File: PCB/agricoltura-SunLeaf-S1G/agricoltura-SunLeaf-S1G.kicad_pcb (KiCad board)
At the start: 2 copper layers, 120 x 40 mm, 84 parts, among them M1 SPSGRFC-915, Q1 DMP3125L-7, Q2 DMP3125L-7, SW1 TL3301NF260QG, T1 BU2032SM-JJ-GTR, T10 BM04B-SRSS-TB(LF)(SN), T11 BM04B-SRSS-TB(LF)(SN), T12 BM04B-SRSS-TB(LF)(SN), T13 BM04B-SRSS-TB(LF)(SN), T14 BM04B-SRSS-TB(LF)(SN), T15 BM04B-SRSS-TB(LF)(SN), T16 BM04B-SRSS-TB(LF)(SN), T17 BM04B-SRSS-TB(LF)(SN), T2 20021121-00010C4LF, T3 0675031020, T4 S2B-PH-K-S(LF)(SN), T5 S3B-PH-K-S(LF)(SN), T6 BM04B-SRSS-TB(LF)(SN), T7 BM04B-SRSS-TB(LF)(SN), T8 BM04B-SRSS-TB(LF)(SN), T9 BM04B-SRSS-TB(LF)(SN), U1 STM32F446RET6, U2 BQ24210DQCT, U3 AZ1117CR-3.3TRG1, U4 TCA9548APWR, U5 74HC4052D, X1 ABM3B-8.000MHZ-B2-T, X2 ABS07-32.768KHZ-9-T

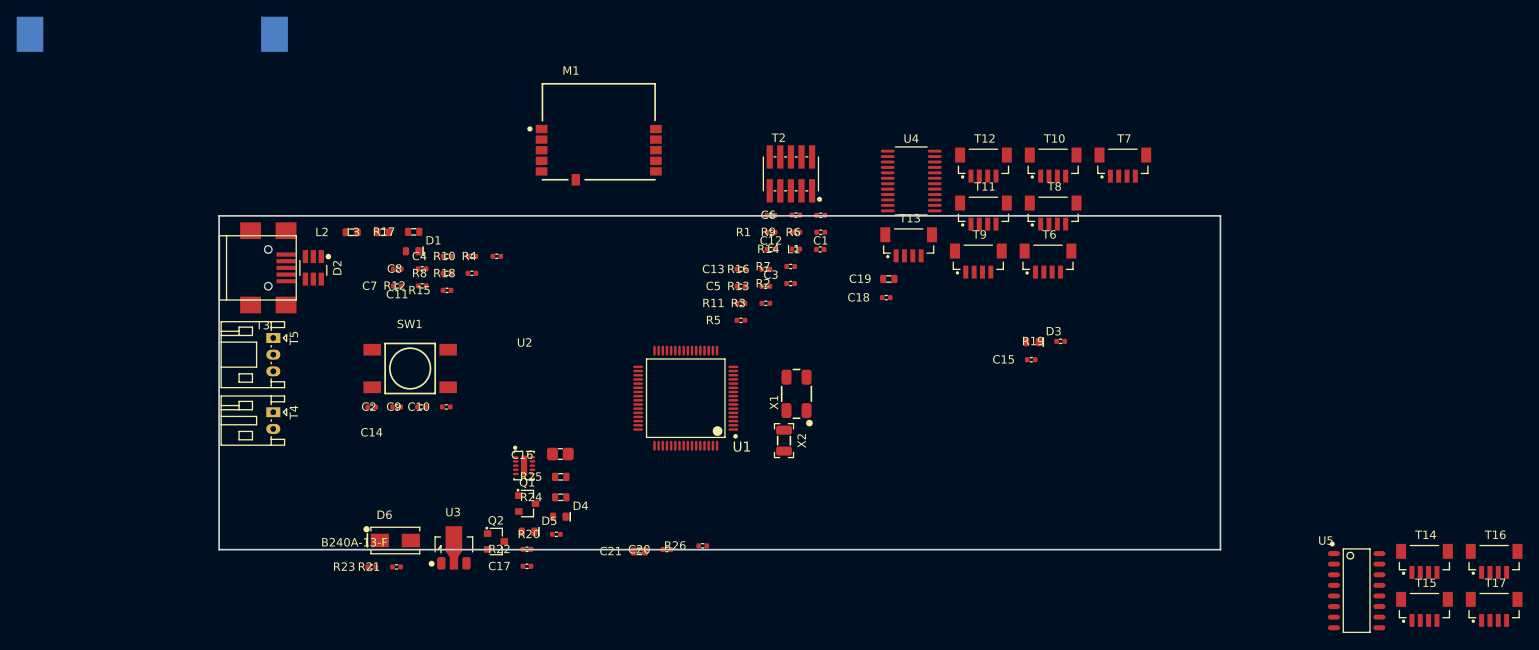
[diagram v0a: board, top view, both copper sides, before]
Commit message: PCB Progress
added TVS diodes fo QWIIC connector serial signals. Did more routing overall.
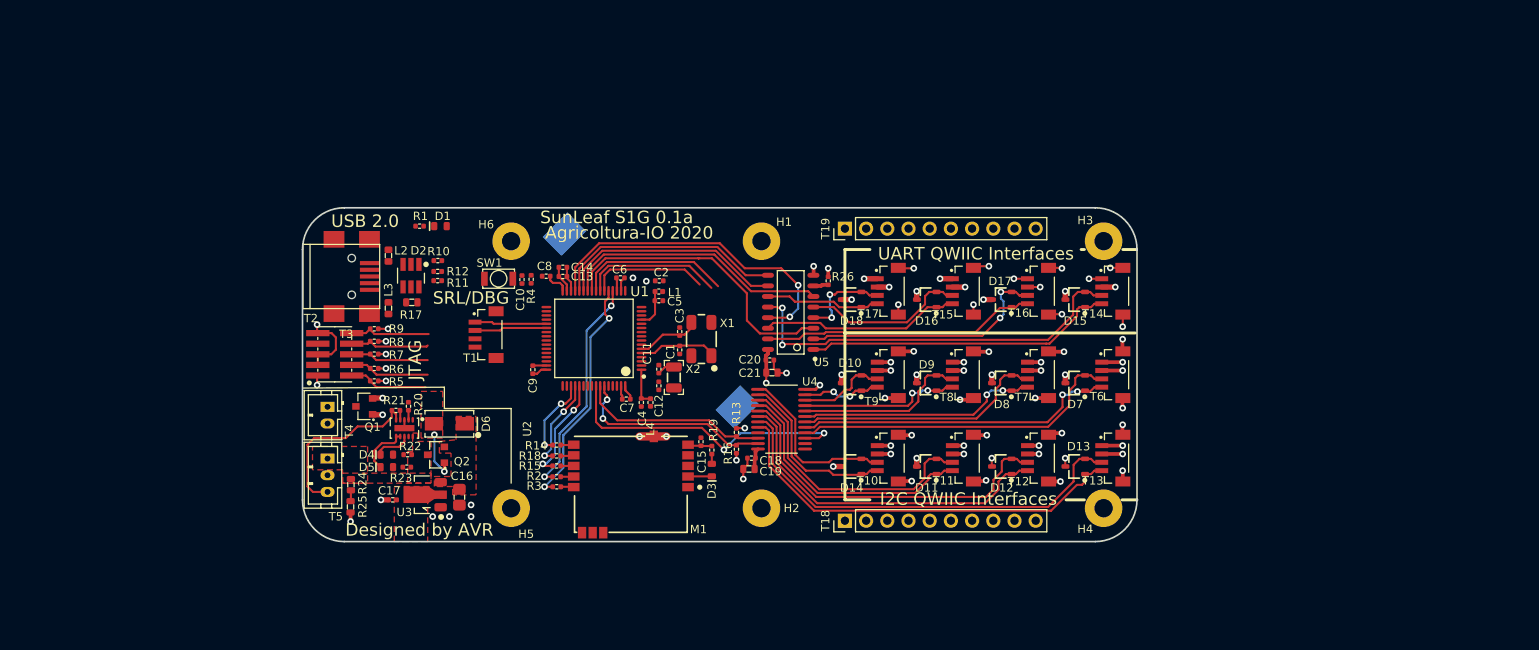
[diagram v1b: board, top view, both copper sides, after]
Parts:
- added D10: PESD3V3L2BT,215, AVR-KiCAD-Lib-Diodes:SOT-23, F.Cu at (165.8, 91.0)
- added D11: PESD3V3L2BT,215, AVR-KiCAD-Lib-Diodes:SOT-23, F.Cu at (174.8, 101.0)
- added D12: PESD3V3L2BT,215, AVR-KiCAD-Lib-Diodes:SOT-23, F.Cu at (183.8, 101.0)
- added D13: PESD3V3L2BT,215, AVR-KiCAD-Lib-Diodes:SOT-23, F.Cu at (192.6, 101.0)
- added D14: PESD3V3L2BT,215, AVR-KiCAD-Lib-Diodes:SOT-23, F.Cu at (165.8, 101.0)
- added D15: PESD3V3L2BT,215, AVR-KiCAD-Lib-Diodes:SOT-23, F.Cu at (192.6, 81.0)
- added D16: PESD3V3L2BT,215, AVR-KiCAD-Lib-Diodes:SOT-23, F.Cu at (174.8, 81.0)
- added D17: PESD3V3L2BT,215, AVR-KiCAD-Lib-Diodes:SOT-23, F.Cu at (183.8, 81.0)
- added D18: PESD3V3L2BT,215, AVR-KiCAD-Lib-Diodes:SOT-23, F.Cu at (165.8, 81.0)
- added D7: PESD3V3L2BT,215, AVR-KiCAD-Lib-Diodes:SOT-23, F.Cu at (192.6, 91.0)
- added D8: PESD3V3L2BT,215, AVR-KiCAD-Lib-Diodes:SOT-23, F.Cu at (183.8, 91.0)
- added D9: PESD3V3L2BT,215, AVR-KiCAD-Lib-Diodes:SOT-23, F.Cu at (174.8, 91.0)
- added H1: M2_Plated_Hole, AVR-KiCAD-Lib-Holes_Fasteners:M2_HOLE, F.Cu at (155.0, 74.0)
- added H2: M2_Plated_Hole, AVR-KiCAD-Lib-Holes_Fasteners:M2_HOLE, F.Cu at (155.0, 106.0)
- added H3: M2_Plated_Hole, AVR-KiCAD-Lib-Holes_Fasteners:M2_HOLE, F.Cu at (196.0, 74.0)
- added H4: M2_Plated_Hole, AVR-KiCAD-Lib-Holes_Fasteners:M2_HOLE, F.Cu at (196.0, 106.0)
- added H5: M2_Plated_Hole, AVR-KiCAD-Lib-Holes_Fasteners:M2_HOLE, F.Cu at (125.0, 106.0)
- added H6: M2_Plated_Hole, AVR-KiCAD-Lib-Holes_Fasteners:M2_HOLE, F.Cu at (125.0, 74.0)
- added L4: BLM15HG601SN1D, AVR-KiCAD-Lib-Inductors:BLM15HG601SN1D, F.Cu at (141.7, 93.3)
- added T18: PPTC101LFBN-RC, AVR-KiCAD-Lib-Connectors:Female_Header_Straight_1x10_Pitch2.54mm, F.Cu at (165.0, 107.5)
- added T19: PPTC101LFBN-RC, AVR-KiCAD-Lib-Connectors:Female_Header_Straight_1x10_Pitch2.54mm, F.Cu at (165.0, 72.5)
- added T20: BU2032SM-JJ-GTR, AVR-KiCAD-Lib-Battery-Holders:BU2032SM-JJ-GTR, B.Cu at (141.8, 83.5)
- M1: value SPSGRFC-915 -> SPSGRF-915
- SW1: value TL3301NF260QG -> B3U-1000P; footprint AVR-KiCAD-Lib-Mech-Switches:TL3301NF260QG -> AVR-KiCAD-Lib-Mech-Switches:B3U-1000P
- T1: value BU2032SM-JJ-GTR -> BM04B-SRSS-TB(LF)(SN); footprint AVR-KiCAD-Lib-Battery-Holders:BU2032SM-JJ-GTR -> AVR-KiCAD-Lib-Connectors:CONN_BM04B-SRSS-TB(LF)(SN); moved to F.Cu
- T4: value S2B-PH-K-S(LF)(SN) -> B2B-PH-K-S(LF)(SN); footprint AVR-KiCAD-Lib-Connectors:S2B-PH-K-S(LF)(SN) -> AVR-KiCAD-Lib-Connectors:B2B-PH-K-S(LF)(SN)
- T5: value S3B-PH-K-S(LF)(SN) -> B3B-PH-K-S(LF)(SN); footprint AVR-KiCAD-Lib-Connectors:S3B-PH-K-S(LF)(SN) -> AVR-KiCAD-Lib-Connectors:B3B-PH-K-S(LF)(SN)
- moved T17 82.0 mm to (170.2, 80.0), turned to 270 degrees
- moved U5 75.6 mm to (158.5, 82.5), turned to 180 degrees
- moved T15 67.1 mm to (179.2, 80.0), turned to 270 degrees
- moved T16 63.5 mm to (188.2, 80.0), turned to 270 degrees
- moved T2 58.8 mm to (103.9, 87.6), turned to 270 degrees
- moved R6 55.9 mm to (108.6, 89.2), turned to 180 degrees
- moved T1 53.8 mm to (122.0, 85.2), turned to 270 degrees
- moved R9 51.8 mm to (108.6, 84.5), turned to 180 degrees
- moved R7 51.0 mm to (108.6, 87.5), turned to 180 degrees
- moved T14 49.4 mm to (197.1, 80.0), turned to 270 degrees
- moved R5 44.5 mm to (108.6, 90.8), turned to 180 degrees
- moved R19 43.8 mm to (149.1, 99.0), turned to 90 degrees
- moved R1 42.1 mm to (114.0, 72.2), turned to 180 degrees
- moved D3 41.4 mm to (149.1, 101.4), turned to 270 degrees
- moved C15 40.8 mm to (147.8, 98.0), turned to 90 degrees
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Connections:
- C11 pad 2: Net-(C11-Pad2) -> /STM32F446RET6 - MCU/OSC32_OUT
- M1 pad 8: /SPSGRF-915 RF Module /RF_SPI_MOSI -> /SPSGRF-915 RF Module /RF_SPI_MISO
- M1 pad 9: (no net) -> /SPSGRF-915 RF Module /RF_SPI_MOSI
- SW1 pad 2: /STM32F446RET6 - MCU/NRST -> GND
- T1 pad 1: /STM32F446RET6 - MCU/VBAT -> /STM32F446RET6 - MCU/DEBUG_UART_TX
- T1 pad 2: GND -> /STM32F446RET6 - MCU/DEBUG_UART_RX
- U1 pad 20: Net-(U1-Pad20) -> /STM32F446RET6 - MCU/CS_MCU
- U1 pad 29: /STM32F446RET6 - MCU/UART_SENSE1_RX -> /STM32F446RET6 - MCU/UART_SENSE1_TX
- U1 pad 37: Net-(U1-Pad37) -> /STM32F446RET6 - MCU/DEBUG_UART_TX
- U1 pad 38: Net-(U1-Pad38) -> /STM32F446RET6 - MCU/DEBUG_UART_RX
- U5 pad 13: /STM32F446RET6 - MCU/UART_SENSE1_RX -> /STM32F446RET6 - MCU/UART_SENSE1_TX
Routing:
- net /STM32F446RET6 - MCU/FGND: track 0.00 -> 239.3 mm
- net GND: track 0.00 -> 89.3 mm, vias 0 -> 51
- net +3V3: track 0.00 -> 59.0 mm, vias 0 -> 34
- net /I2C Mux & Connections/QWIIC_SD7: track 0.00 -> 51.6 mm
- net /I2C Mux & Connections/QWIIC_SC7: track 0.00 -> 50.5 mm
- net /UART Mux & Connections/UARTS1_TX: track 0.00 -> 48.5 mm, vias 0 -> 2
- net /I2C Mux & Connections/QWIIC_SD6: track 0.00 -> 42.5 mm
- net /I2C Mux & Connections/QWIIC_SC6: track 0.00 -> 41.3 mm
- net /I2C Mux & Connections/QWIIC_SD0: track 0.00 -> 40.1 mm
- net /STM32F446RET6 - MCU/UART_SENSE1_TX: track 0.00 -> 39.7 mm, vias 0 -> 2
- net /I2C Mux & Connections/QWIIC_SC0: track 0.00 -> 38.4 mm, vias 0 -> 2
- net /UART Mux & Connections/UARTS1_RX: track 0.00 -> 37.3 mm
- net /I2C Mux & Connections/I2C_MUX1_RESET: track 0.00 -> 36.4 mm, vias 0 -> 2
- net /STM32F446RET6 - MCU/UART_SENSE1_RX: track 0.00 -> 35.5 mm
- net /UART Mux & Connections/UARTS3_RX: track 0.00 -> 33.1 mm
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- added copper zone on F.Cu, net (none)
- added copper zone on F.Cu, net +3V3
- added copper zone on In2.Cu, net +3V3
- added copper zone on F.Cu, net /Power Supply & Battery Charging/3V3_REG_IN
- added copper zone on F.Cu, net /Power Supply & Battery Charging/BAT
- added copper zone on F.Cu, net /Power Supply & Battery Charging/USB_VBUS
- added copper zone on In2.Cu, net /Power Supply & Battery Charging/USB_VBUS
- added copper zone on In1.Cu, net GND
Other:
- board size 120 x 40 mm -> 100 x 40 mm
- copper layers 2 -> 4
- rule trace_min: 0.2 -> 0.1778
- board text added: "Agricoltura-IO 2020"
- board text added: "Designed by AVR"
- board text added: "I2C QWIIC Interfaces"
- board text added: "JTAG"
- board text added: "SRL/DBG"
- board text added: "SunLeaf S1G 0.1a"
- board text added: "UART QWIIC Interfaces"
- board text added: "USB 2.0"

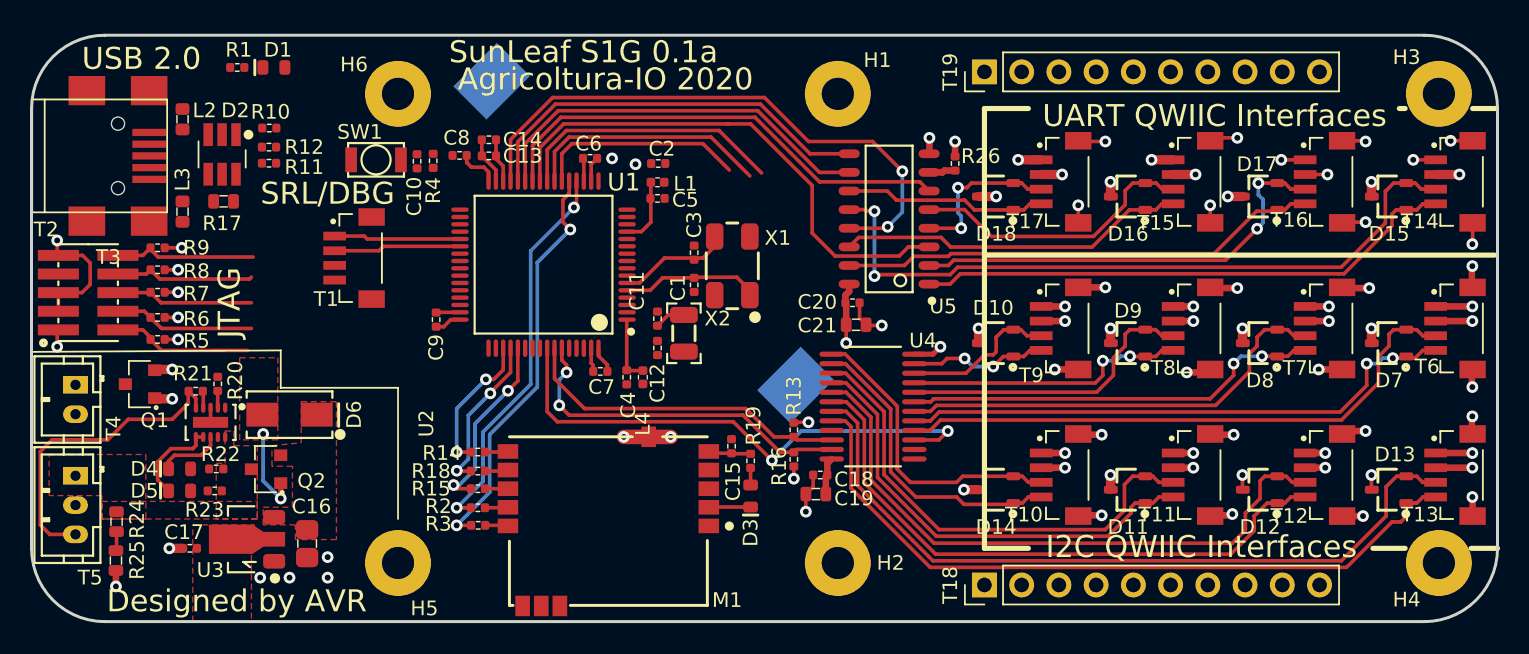
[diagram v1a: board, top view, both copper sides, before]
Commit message: Pullups
Added pullup reistors to I2C ports, changed JTAG connector over to Tag connect.
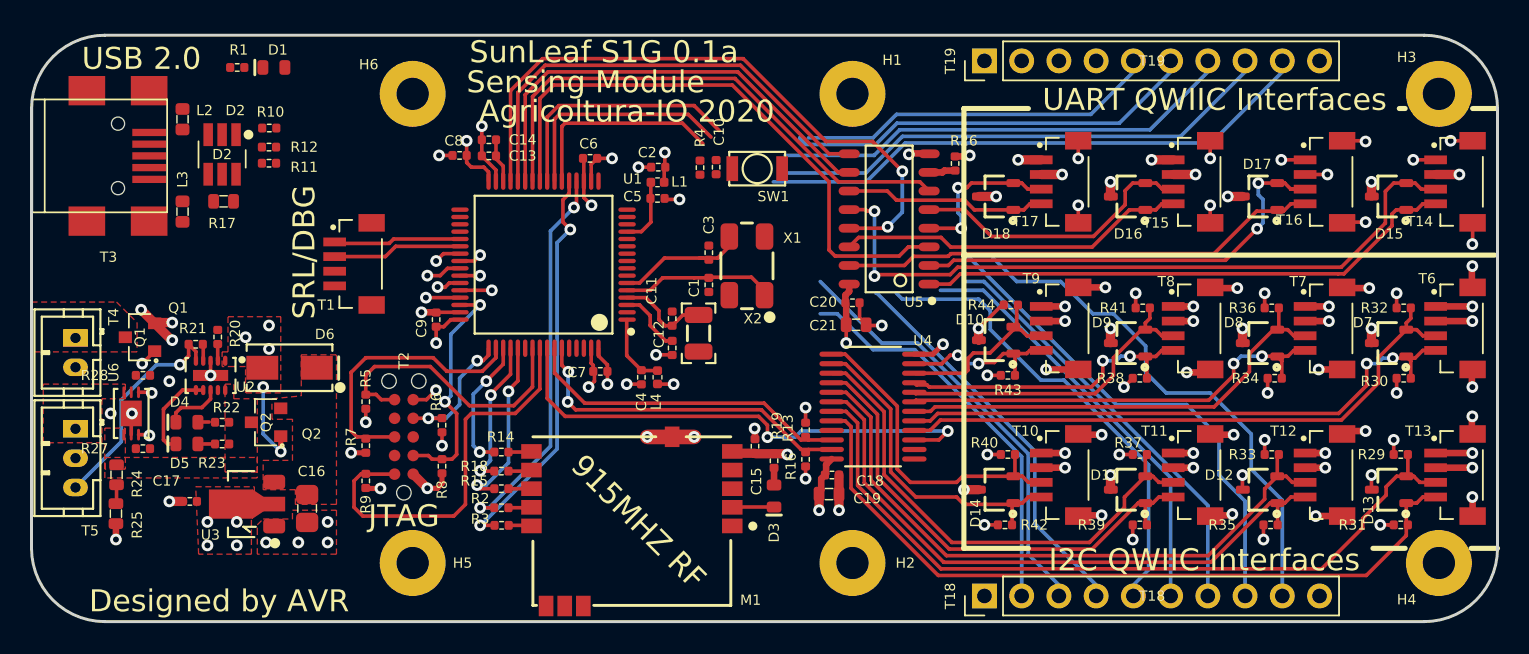
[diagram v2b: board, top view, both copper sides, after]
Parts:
- removed T20: BU2032SM-JJ-GTR, AVR-KiCAD-Lib-Battery-Holders:BU2032SM-JJ-GTR
- added R27: RC0402FR-074K7L, AVR-KiCAD-Lib-Resistors:R0402, F.Cu at (107.6, 98.2)
- added R28: RC0402FR-074K7L, AVR-KiCAD-Lib-Resistors:R0402, F.Cu at (107.6, 93.2)
- added R29: RC0402FR-074K7L, AVR-KiCAD-Lib-Resistors:R0402, F.Cu at (193.4, 98.6)
- added R30: RC0402FR-074K7L, AVR-KiCAD-Lib-Resistors:R0402, F.Cu at (193.6, 93.4)
- added R31: RC0402FR-074K7L, AVR-KiCAD-Lib-Resistors:R0402, F.Cu at (193.4, 103.4)
- added R32: RC0402FR-074K7L, AVR-KiCAD-Lib-Resistors:R0402, F.Cu at (193.6, 88.6)
- added R33: RC0402FR-074K7L, AVR-KiCAD-Lib-Resistors:R0402, F.Cu at (184.6, 98.6)
- added R34: RC0402FR-074K7L, AVR-KiCAD-Lib-Resistors:R0402, F.Cu at (184.8, 93.4)
- added R35: RC0402FR-074K7L, AVR-KiCAD-Lib-Resistors:R0402, F.Cu at (184.5, 103.4)
- added R36: RC0402FR-074K7L, AVR-KiCAD-Lib-Resistors:R0402, F.Cu at (184.6, 88.6)
- added R37: RC0402FR-074K7L, AVR-KiCAD-Lib-Resistors:R0402, F.Cu at (175.6, 98.6)
- added R38: RC0402FR-074K7L, AVR-KiCAD-Lib-Resistors:R0402, F.Cu at (175.6, 93.4)
- added R39: RC0402FR-074K7L, AVR-KiCAD-Lib-Resistors:R0402, F.Cu at (175.6, 103.4)
- added R40: RC0402FR-074K7L, AVR-KiCAD-Lib-Resistors:R0402, F.Cu at (166.6, 98.6)
- added R41: RC0402FR-074K7L, AVR-KiCAD-Lib-Resistors:R0402, F.Cu at (175.8, 88.6)
- added R42: RC0402FR-074K7L, AVR-KiCAD-Lib-Resistors:R0402, F.Cu at (166.4, 103.4)
- added R43: RC0402FR-074K7L, AVR-KiCAD-Lib-Resistors:R0402, F.Cu at (166.6, 93.2)
- added R44: RC0402FR-074K7L, AVR-KiCAD-Lib-Resistors:R0402, F.Cu at (166.8, 88.4)
- added U6: LTC2941CDCB-1#TRMPBF, AVR-KiCAD-Lib-ICs:LTC2941CDCB-1-TRMPBF, F.Cu at (106.8, 95.8)
- T2: value 20021121-00010C4LF -> TC2050-IDC-NL-FP; footprint AVR-KiCAD-Lib-Connectors:20021121-00010C4LF -> AVR-KiCAD-Lib-Connectors:TC2050-CLIP
- moved SW1 26.0 mm to (149.5, 79.1), turned to 0 degrees
- moved T2 23.7 mm to (125.4, 97.4), turned to 90 degrees
- moved R8 23.6 mm to (128.0, 99.4), turned to 90 degrees
- moved R9 21.3 mm to (122.8, 100.4), turned to 90 degrees
- moved R6 20.7 mm to (128.0, 96.6), turned to 90 degrees
- moved C10 20.4 mm to (146.7, 79.0), turned to 270 degrees
- moved R4 18.2 mm to (145.6, 79.0), turned to 90 degrees
- moved R7 17.6 mm to (122.8, 98.0), turned to 90 degrees
- moved R5 14.8 mm to (122.8, 95.0), turned to 90 degrees
- moved D5 3.24 mm to (110.6, 97.9)
- moved R23 3.24 mm to (113.0, 97.9)
- moved D4 3.22 mm to (110.6, 96.4)
- moved R22 3.21 mm to (113.0, 96.4)
- moved C17 3.20 mm to (110.8, 101.8)
- moved D6 3.20 mm to (117.6, 92.7)
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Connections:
- R5 pad 2: /STM32F446RET6 - MCU/SWDIO_TMS -> /STM32F446RET6 - MCU/SWO_TDO
- R7 pad 2: /STM32F446RET6 - MCU/SWO_TDO -> /STM32F446RET6 - MCU/SWO_TDI
- R8 pad 2: /STM32F446RET6 - MCU/SWO_TDI -> /STM32F446RET6 - MCU/SWDIO_TMS
- T18 pad 10: Net-(T18-Pad10) -> GND
- T2 pad 3: GND -> Net-(T2-Pad3)
- T2 pad 9: GND -> Net-(T2-Pad9)
- T5 pad 1: /Power Supply & Battery Charging/BAT -> Net-(T5-Pad1)
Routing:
- net Net-(T19-Pad9): track 0.00 -> 37.8 mm
- net Net-(T18-Pad9): track 0.00 -> 34.8 mm
- net Net-(T19-Pad8): track 0.00 -> 34.2 mm
- net Net-(T18-Pad8): track 0.00 -> 33.3 mm
- net Net-(T18-Pad5): track 0.00 -> 31.4 mm
- net Net-(T19-Pad7): track 0.00 -> 31.2 mm
- net Net-(T18-Pad3): track 0.00 -> 28.9 mm
- net Net-(T18-Pad7): track 0.00 -> 28.4 mm
- net Net-(T18-Pad6): track 0.00 -> 28.3 mm
- net +3V3: track 59.0 -> 87.3 mm, vias 34 -> 60
- net Net-(T19-Pad6): track 0.00 -> 27.6 mm
- net Net-(T18-Pad2): track 0.00 -> 26.5 mm
- net Net-(T18-Pad4): track 0.00 -> 26.2 mm
- net Net-(T19-Pad5): track 0.00 -> 24.0 mm
- net /STM32F446RET6 - MCU/NJTRST: track 9.77 -> 27.4 mm
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- added copper zone on F.Cu, net /Power Supply & Battery Charging/Solar_PNL
- added copper zone on F.Cu, net GND
- added copper zone on F.Cu, net Net-(T5-Pad1)
- removed copper zone on F.Cu, net (none)
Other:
- board text added: "3V3"
- board text added: "915MHZ RF"
- board text added: "915MHZ RF Sensing Module"
- board text added: "Designed by Adam Vadala-Roth"
- board text added: "GND"
- board text added: "GPIO0"
- board text added: "GPIO1"
- board text added: "GPIO10"
- board text added: "GPIO11"
- board text added: "GPIO12"
- board text added: "GPIO13"
- board text added: "GPIO14"
- board text added: "GPIO15"
- board text added: "GPIO2"
- board text added: "GPIO3"
- board text added: "GPIO4"
- board text added: "GPIO5"
- board text added: "GPIO6"
- board text added: "GPIO7"
- board text added: "GPIO8"
- board text added: "GPIO9"
- board text added: "Sensing Module"
